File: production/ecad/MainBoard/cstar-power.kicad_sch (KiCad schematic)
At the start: 48 parts, among them IC1 LT8648SEV#PBF, J1 Conn_01x02_Pin, J2 Conn_01x02_Pin, J3 Conn_01x02_Pin, J4 XT60PW-M, U1 AZ1117IH-3.3TRG1

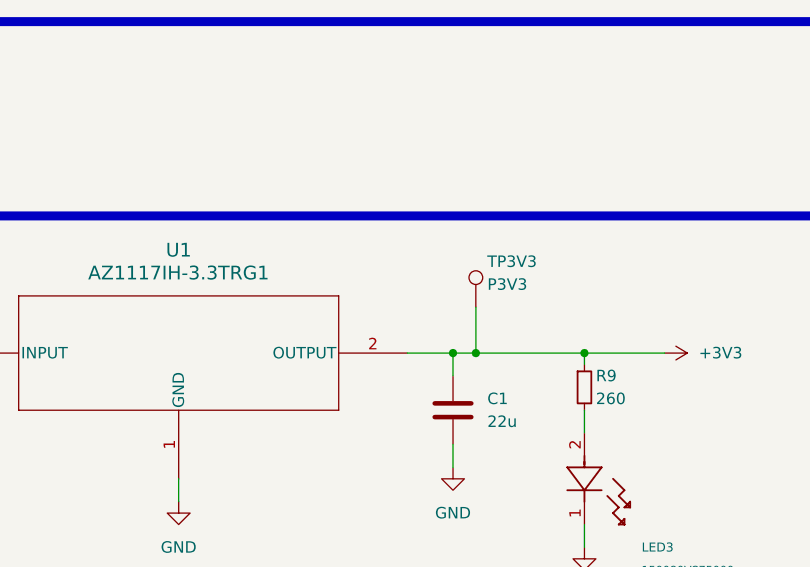
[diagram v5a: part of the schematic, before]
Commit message: component placement
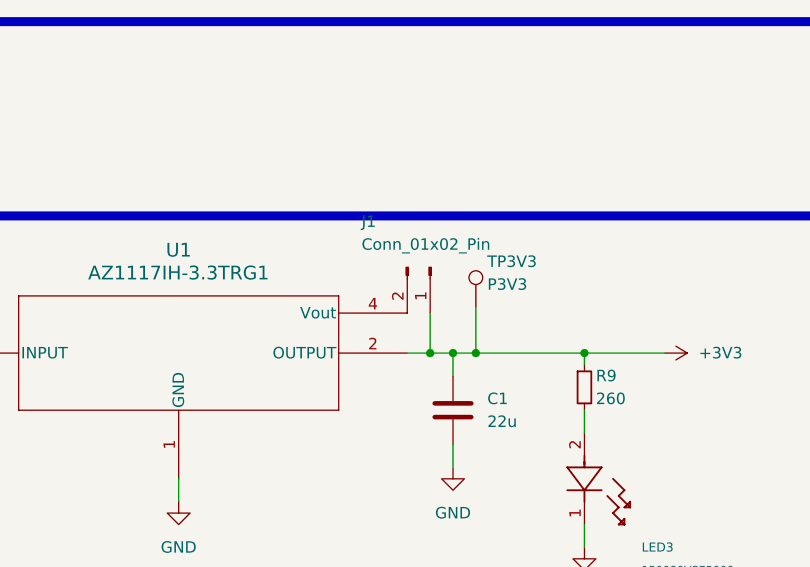
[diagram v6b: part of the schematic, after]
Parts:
- added J1: Conn_01x02_Pin, Connector_PinHeader_2.54mm:PinHeader_1x02_P2.54mm_Vertical, symbol Connector:Conn_01x02_Pin
- U1: footprint CSTAR-MainBoard-Footprints:TO252-2_AZ1117ID-3.3TRG1_DIO -> CSTAR-MainBoard-Footprints:SOT230P700X185-4N
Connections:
- net +3V3: now also J1.1 (Pin_1)
- new net: J1.2 (Pin_2), U1.4 (Vout)
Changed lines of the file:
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@@
   (junction (at 199.39 92.71) (diameter 0) (color 0 0 0 0)
+  )
+  (junction (at 140.97 175.26) (diameter 0) (color 0 0 0 0)
   )
   (no_connect (at 299.72 187.96))
@@
     (stroke (width 0) (type default))
   )
-  (wire (pts (xy 138.43 175.26) (xy 143.51 175.26))
+  (wire (pts (xy 138.43 175.26) (xy 140.97 175.26))
     (stroke (width 0) (type default))
   )
@@
     (stroke (width 0) (type default))
   )
+  (wire (pts (xy 140.97 170.815) (xy 140.97 175.26))
+    (stroke (width 0) (type default))
+  )
   (wire (pts (xy 147.32 123.19) (xy 147.32 125.73))
     (stroke (width 0) (type default))
@@
   )
   (wire (pts (xy 97.79 87.63) (xy 97.79 93.98))
+    (stroke (width 0) (type default))
+  )
+  (wire (pts (xy 140.97 175.26) (xy 143.51 175.26))
     (stroke (width 0) (type default))
   )
@@
     )
   )
+  (symbol (lib_id "Connector:Conn_01x02_Pin") (at 140.97 165.735 270) (unit 1)
+    (in_bom yes) (on_board yes) (dnp no)
+    (property "Reference" "J1" (at 133.35 160.655 90)
+      (effects (font (size 1.27 1.27)) (justify left))
+    )
+    (property "Value" "Conn_01x02_Pin" (at 133.35 163.195 90)
+      (effects (font (size 1.27 1.27)) (justify left))
+    )
+    (property "Footprint" "Connector_PinHeader_2.54mm:PinHeader_1x02_P2.54mm_Vertical" (at 140.97 165.735 0)
+      (effects (font (size 1.27 1.27)) hide)
+    )
+    (property "Datasheet" "~" (at 140.97 165.735 0)
+      (effects (font (size 1.27 1.27)) hide)
+    )
+    (pin "1")
+    (pin "2")
+    (instances
+      (project "cstar-power"
+        (path "/7edd775e-47a6-46f9-8e16-808bdf3a0e15"
+          (reference "J1") (unit 1)
+        )
+      )
+      (project "CSTAR"
+        (path "/cd9fa943-c6eb-468b-990c-ea873c442553/0fc3a7ee-d954-4a57-b160-08f1c7c2ed5e"
+          (reference "J23") (unit 1)
+        )
+      )
+    )
+  )
   (symbol (lib_id "Device:R_Small") (at 115.57 110.49 0) (unit 1)
     (in_bom yes) (on_board yes) (dnp no)
@@
       (effects (font (size 1.524 1.524)))
     )
-    (property "Footprint" "CSTAR-MainBoard-Footprints:TO252-2_AZ1117ID-3.3TRG1_DIO" (at 83.82 154.94 0)
+    (property "Footprint" "CSTAR-MainBoard-Footprints:SOT230P700X185-4N" (at 83.82 154.94 0)
       (effects (font (size 1.27 1.27) italic) hide)
     )
@@
     (pin "1")
     (pin "3")
-    (instances
-      (project "cstar-power"
+    (pin "4")
+    (instances
+      (project "cstar-power"

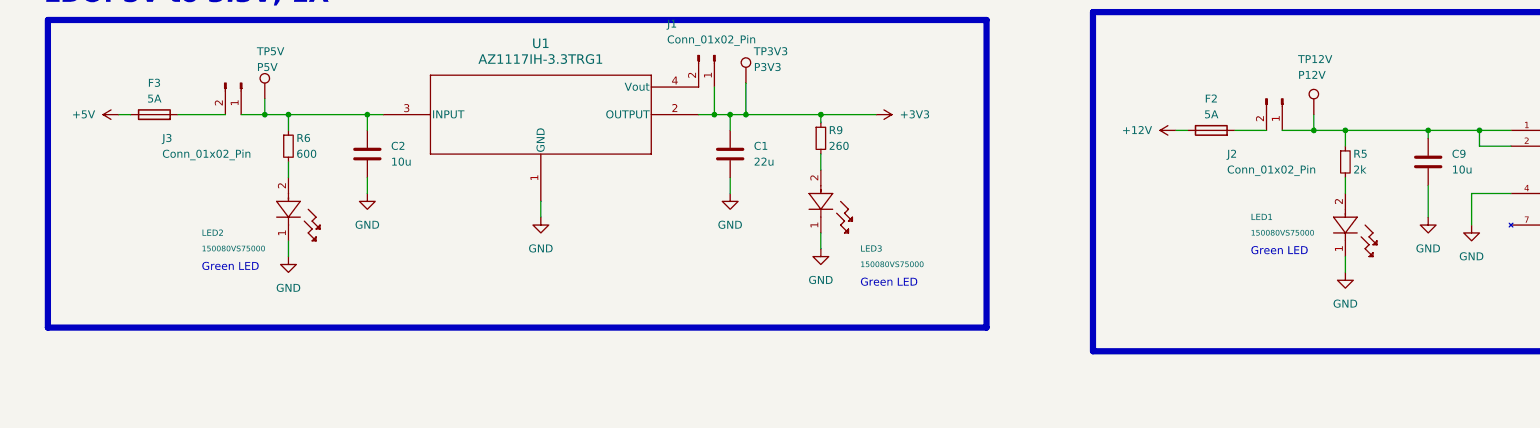
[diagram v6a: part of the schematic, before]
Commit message: moved LEDs before the fuse
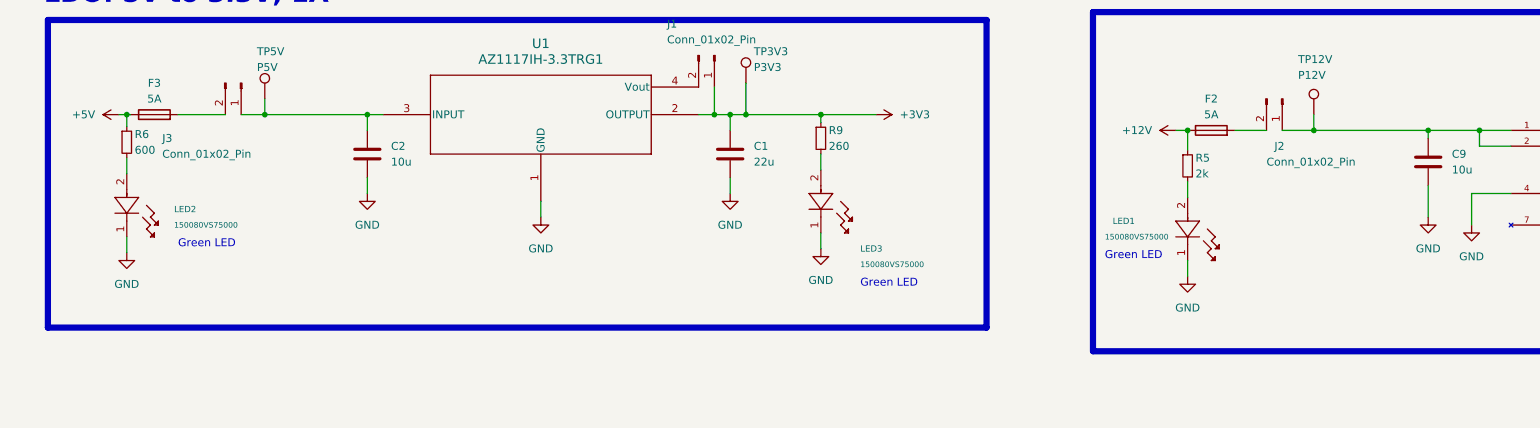
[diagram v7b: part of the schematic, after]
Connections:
- net +12V: now also R5.1
- net +5V: now also R6.1
- net at C2.1, J3.1 (Pin_1), TP5V.1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: no longer R6.1
- net at C9.1, J2.1 (Pin_1), PS1.1 (VIN)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: no longer R5.1
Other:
- moved on the sheet: LED1, LED2, R5, R6

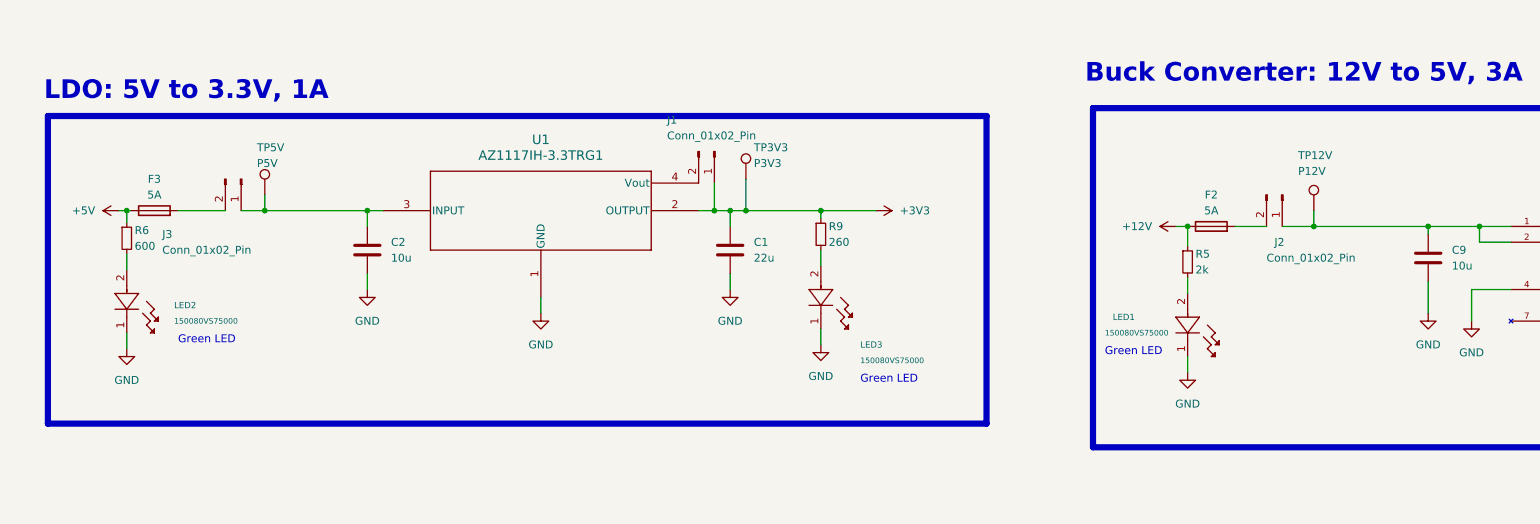
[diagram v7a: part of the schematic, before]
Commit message: "Added Backup Connector"
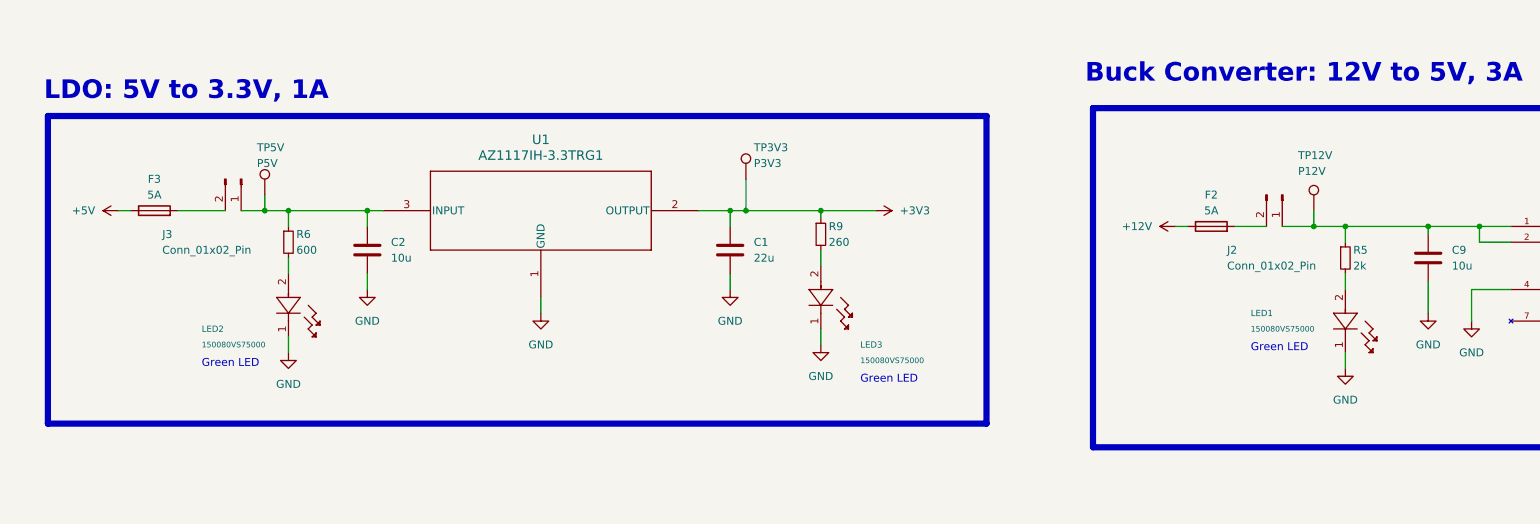
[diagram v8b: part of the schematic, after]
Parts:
- removed J1: Conn_01x02_Pin, Connector_PinHeader_2.54mm:PinHeader_1x02_P2.54mm_Vertical, symbol Connector:Conn_01x02_Pin
- C6, C7: footprint Capacitor_SMD:C_1206_3216Metric -> Capacitor_SMD:C_0805_2012Metric
- L1: footprint CSTAR-MainBoard-Footprints:L1_2.2uH -> Inductor_SMD:L_0805_2012Metric
- L2: footprint CSTAR-MainBoard-Footprints:L2_6.8uH -> Inductor_SMD:L_0805_2012Metric
- U1: footprint CSTAR-MainBoard-Footprints:SOT230P700X185-4N -> CSTAR-MainBoard-Footprints:TO252-2_AZ1117ID-3.3TRG1_DIO
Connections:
- net +12V: no longer R5.1
- net +5V: no longer R6.1
- net at C2.1, J3.1 (Pin_1), TP5V.1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: now also R6.1
- net at C9.1, J2.1 (Pin_1), PS1.1 (VIN)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: now also R5.1
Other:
- moved on the sheet: LED1, LED2, R5, R6
